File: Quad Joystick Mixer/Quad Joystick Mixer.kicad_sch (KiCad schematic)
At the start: 0 parts

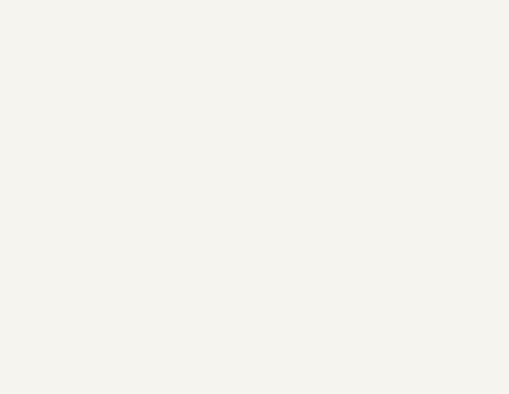
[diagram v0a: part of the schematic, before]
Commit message: work on audio input circuit
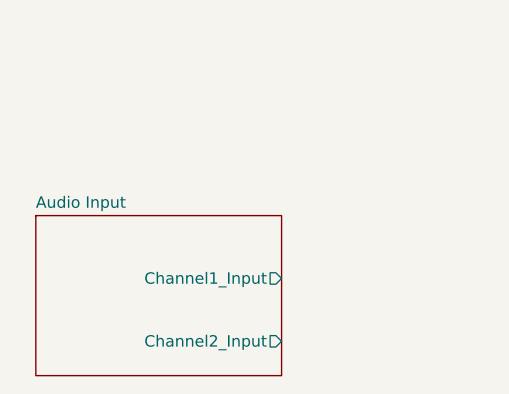
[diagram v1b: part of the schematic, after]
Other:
- added sheet Audio Input (audioInput.kicad_sch)
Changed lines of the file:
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@@
+    )
+  )
+  (sheet (at 59.055 127.635) (size 27.305 17.78) (fields_autoplaced)
+    (stroke (width 0.1524) (type solid))
+    (fill (color 0 0 0 0.0000))
+    (property "Sheetname" "Audio Input" (at 59.055 126.9234 0)
+      (effects (font (size 1.27 1.27)) (justify left bottom))
+    )
+    (property "Sheetfile" "audioInput.kicad_sch" (at 59.055 145.9996 0)
+      (effects (font (size 1.27 1.27)) (justify left top) hide)
+    )
+    (pin "Channel2_Input" output (at 86.36 141.605 0)
+      (effects (font (size 1.27 1.27)) (justify right))
+    )
+    (pin "Channel1_Input" output (at 86.36 134.62 0)
+      (effects (font (size 1.27 1.27)) (justify right))
+    )
+    (instances
+      (project "Quad Joystick Mixer"
+        (path "/e9da4955-68c1-4335-ab8e-8a9cc0328d2d" (page "3"))
+      )
     )
   )

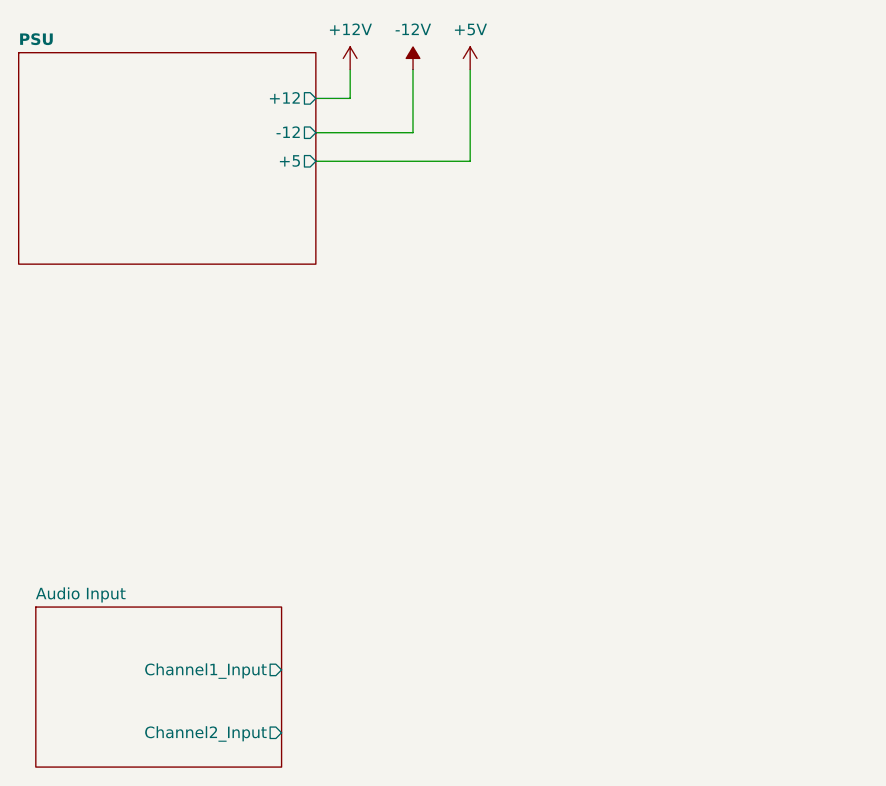
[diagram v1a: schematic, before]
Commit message: add analog 5V rail
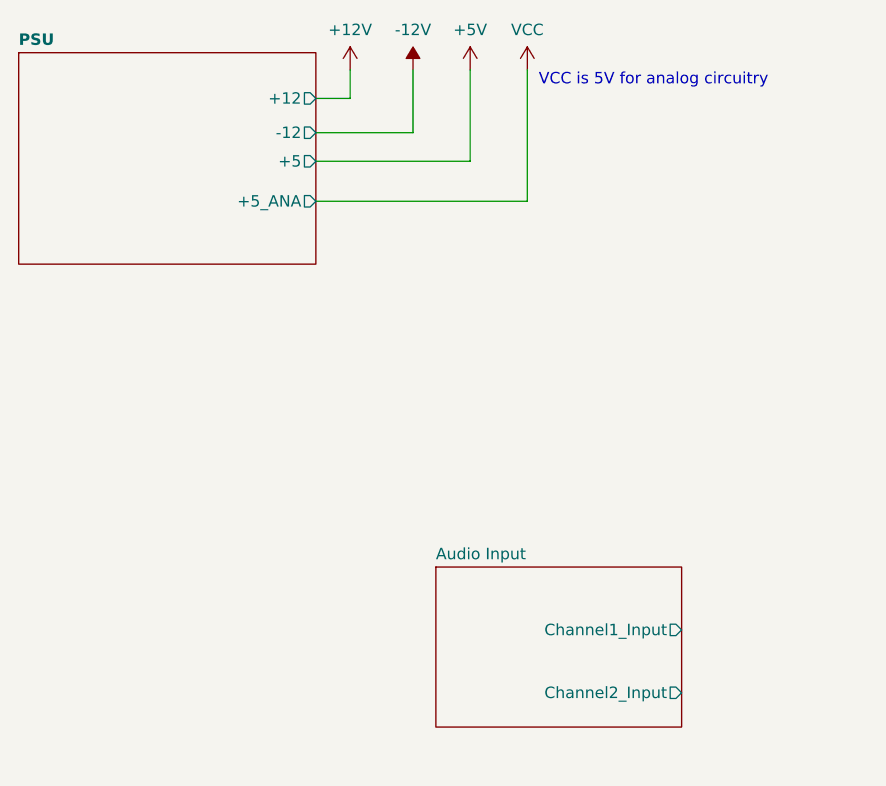
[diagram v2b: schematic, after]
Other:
- sheet PSU ports: added +5_ANA; removed none
- note added: "VCC is 5V for analog circuitry"
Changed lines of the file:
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@@
     (rev "P1")
+  )
+  (wire (pts (xy 90.17 82.55) (xy 113.665 82.55))
+    (stroke (width 0) (type default))
   )
   (wire (pts (xy 90.17 71.12) (xy 93.98 71.12))
@@
   )
   (wire (pts (xy 93.98 71.12) (xy 93.98 67.945))
+    (stroke (width 0) (type default))
+  )
+  (wire (pts (xy 113.665 82.55) (xy 113.665 67.945))
     (stroke (width 0) (type default))
   )
@@
     )
   )
+  (text "VCC is 5V for analog circuitry" (at 114.935 69.85 0)
+    (effects (font (size 1.27 1.27)) (justify left bottom))
+  )
   (symbol (lib_id "power:+5V") (at 107.315 67.945 0) (unit 1)
     (in_bom yes) (on_board yes) (dnp no)
@@
     )
   )
+  (symbol (lib_id "power:VCC") (at 113.665 67.945 0) (unit 1)
+    (in_bom yes) (on_board yes) (dnp no) (fields_autoplaced)
+    (property "Reference" "#PWR013" (at 113.665 71.755 0)
+      (effects (font (size 1.27 1.27)) hide)
+    )
+    (property "Value" "VCC" (at 113.665 63.5 0)
+      (effects (font (size 1.27 1.27)))
+    )
+    (property "Footprint" "" (at 113.665 67.945 0)
+      (effects (font (size 1.27 1.27)) hide)
+    )
+    (property "Datasheet" "" (at 113.665 67.945 0)
+      (effects (font (size 1.27 1.27)) hide)
+    )
+    (pin "1")
+    (instances
+      (project "Quad Joystick Mixer"
+        (path "/e9da4955-68c1-4335-ab8e-8a9cc0328d2d"
+          (reference "#PWR013") (unit 1)
+        )
+      )
+    )
+  )
   (sheet (at 57.15 66.04) (size 33.02 23.495) (fields_autoplaced)
     (stroke (width 0.1524) (type solid))
@@
       (effects (font (size 1.27 1.27)) (justify right))
     )
+    (pin "+5_ANA" output (at 90.17 82.55 0)
+      (effects (font (size 1.27 1.27)) (justify right))
+    )
     (instances
       (project "Quad Joystick Mixer"
@@
     )
   )
-  (sheet (at 59.055 127.635) (size 27.305 17.78) (fields_autoplaced)
+  (sheet (at 103.505 123.19) (size 27.305 17.78) (fields_autoplaced)
     (stroke (width 0.1524) (type solid))
     (fill (color 0 0 0 0.0000))
-    (property "Sheetname" "Audio Input" (at 59.055 126.9234 0)
+    (property "Sheetname" "Audio Input" (at 103.505 122.4784 0)
       (effects (font (size 1.27 1.27)) (justify left bottom))
     )
-    (property "Sheetfile" "audioInput.kicad_sch" (at 59.055 145.9996 0)
+    (property "Sheetfile" "audioInput.kicad_sch" (at 103.505 141.5546 0)
       (effects (font (size 1.27 1.27)) (justify left top) hide)
     )
-    (pin "Channel2_Input" output (at 86.36 141.605 0)
+    (pin "Channel2_Input" output (at 130.81 137.16 0)
       (effects (font (size 1.27 1.27)) (justify right))
     )
-    (pin "Channel1_Input" output (at 86.36 134.62 0)
+    (pin "Channel1_Input" output (at 130.81 130.175 0)
       (effects (font (size 1.27 1.27)) (justify right))
     )

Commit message: more progress on schematic
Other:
- added sheet Digital Pot (digitalPot.kicad_sch)
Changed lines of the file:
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@@
+    )
+  )
+  (sheet (at 168.91 120.65) (size 28.575 19.685) (fields_autoplaced)
+    (stroke (width 0.1524) (type solid))
+    (fill (color 0 0 0 0.0000))
+    (property "Sheetname" "Digital Pot" (at 168.91 119.9384 0)
+      (effects (font (size 1.27 1.27)) (justify left bottom))
+    )
+    (property "Sheetfile" "digitalPot.kicad_sch" (at 168.91 140.9196 0)
+      (effects (font (size 1.27 1.27)) (justify left top) hide)
+    )
+    (instances
+      (project "Quad Joystick Mixer"
+        (path "/e9da4955-68c1-4335-ab8e-8a9cc0328d2d" (page "4"))
+      )
     )
   )

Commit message: work through digital pot circuit
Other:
- sheet Digital Pot renamed Channel 1 Digital Pots
- sheet Channel 1 Digital Pots ports: added Input, OUTA, OUTB, OUTC, OUTD, SCL, SDA; removed none
- note added: "AB address 0b000 CD address 0b001"
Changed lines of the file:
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@@
+    (stroke (width 0) (type default))
+  )
+  (wire (pts (xy 130.81 130.175) (xy 159.385 130.175))
     (stroke (width 0) (type default))
   )
@@
     )
   )
+  (text "AB address 0b000\nCD address 0b001" (at 160.655 139.065 0)
+    (effects (font (size 1.27 1.27)) (justify left bottom))
+  )
   (text "VCC is 5V for analog circuitry" (at 114.935 69.85 0)
     (effects (font (size 1.27 1.27)) (justify left bottom))
@@
     )
   )
-  (sheet (at 168.91 120.65) (size 28.575 19.685) (fields_autoplaced)
+  (sheet (at 159.385 120.015) (size 28.575 19.685) (fields_autoplaced)
     (stroke (width 0.1524) (type solid))
     (fill (color 0 0 0 0.0000))
-    (property "Sheetname" "Digital Pot" (at 168.91 119.9384 0)
+    (property "Sheetname" "Channel 1 Digital Pots" (at 159.385 119.3034 0)
       (effects (font (size 1.27 1.27)) (justify left bottom))
     )
-    (property "Sheetfile" "digitalPot.kicad_sch" (at 168.91 140.9196 0)
+    (property "Sheetfile" "digitalPot.kicad_sch" (at 159.385 140.2846 0)
       (effects (font (size 1.27 1.27)) (justify left top) hide)
     )
+    (pin "Input" input (at 159.385 130.175 180)
+      (effects (font (size 1.27 1.27)) (justify left))
+    )
+    (pin "SDA" bidirectional (at 159.385 126.365 180)
+      (effects (font (size 1.27 1.27)) (justify left))
+    )
+    (pin "SCL" input (at 159.385 123.19 180)
+      (effects (font (size 1.27 1.27)) (justify left))
+    )
+    (pin "OUTA" output (at 187.96 123.825 0)
+      (effects (font (size 1.27 1.27)) (justify right))
+    )
+    (pin "OUTB" output (at 187.96 127.635 0)
+      (effects (font (size 1.27 1.27)) (justify right))
+    )
+    (pin "OUTD" output (at 187.96 135.255 0)
+      (effects (font (size 1.27 1.27)) (justify right))
+    )
+    (pin "OUTC" output (at 187.96 131.445 0)
+      (effects (font (size 1.27 1.27)) (justify right))
+    )
     (instances

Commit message: working on finishing a draft of this dang schematic
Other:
- added sheet Audio Output (audioOutput.kicad_sch)
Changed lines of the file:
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@@
+    (stroke (width 0) (type default))
+  )
+  (wire (pts (xy 187.96 131.445) (xy 224.79 131.445))
     (stroke (width 0) (type default))
   )
@@
     (stroke (width 0) (type default))
   )
+  (wire (pts (xy 187.96 123.825) (xy 224.79 123.825))
+    (stroke (width 0) (type default))
+  )
   (wire (pts (xy 100.965 67.945) (xy 100.965 74.93))
     (stroke (width 0) (type default))
@@
   )
   (wire (pts (xy 90.17 78.105) (xy 107.315 78.105))
+    (stroke (width 0) (type default))
+  )
+  (wire (pts (xy 187.96 135.255) (xy 224.79 135.255))
+    (stroke (width 0) (type default))
+  )
+  (wire (pts (xy 187.96 127.635) (xy 224.79 127.635))
     (stroke (width 0) (type default))
   )
@@
       )
     )
+  )
+  (sheet (at 224.79 120.015) (size 28.575 19.05) (fields_autoplaced)
+    (stroke (width 0.1524) (type solid))
+    (fill (color 0 0 0 0.0000))
+    (property "Sheetname" "Audio Output" (at 224.79 119.3034 0)
+      (effects (font (size 1.27 1.27)) (justify left bottom))
+    )
+    (property "Sheetfile" "audioOutput.kicad_sch" (at 224.79 139.6496 0)
+      (effects (font (size 1.27 1.27)) (justify left top) hide)
+    )
+    (pin "A" input (at 224.79 123.825 180)
+      (effects (font (size 1.27 1.27)) (justify left))
+    )
+    (pin "B" input (at 224.79 127.635 180)
+      (effects (font (size 1.27 1.27)) (justify left))
+    )
+    (pin "C" input (at 224.79 131.445 180)
+      (effects (font (size 1.27 1.27)) (justify left))
+    )
+    (pin "D" input (at 224.79 135.255 180)
+      (effects (font (size 1.27 1.27)) (justify left))
+    )
+    (instances
+      (project "Quad Joystick Mixer"
+        (path "/e9da4955-68c1-4335-ab8e-8a9cc0328d2d" (page "5"))
+      )
+    )
